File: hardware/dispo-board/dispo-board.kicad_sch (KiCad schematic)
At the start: 22 parts, among them SW1 SW_Push, U1 STM32H725RGV6, U2 TPS79633DCQ, Y1 32M

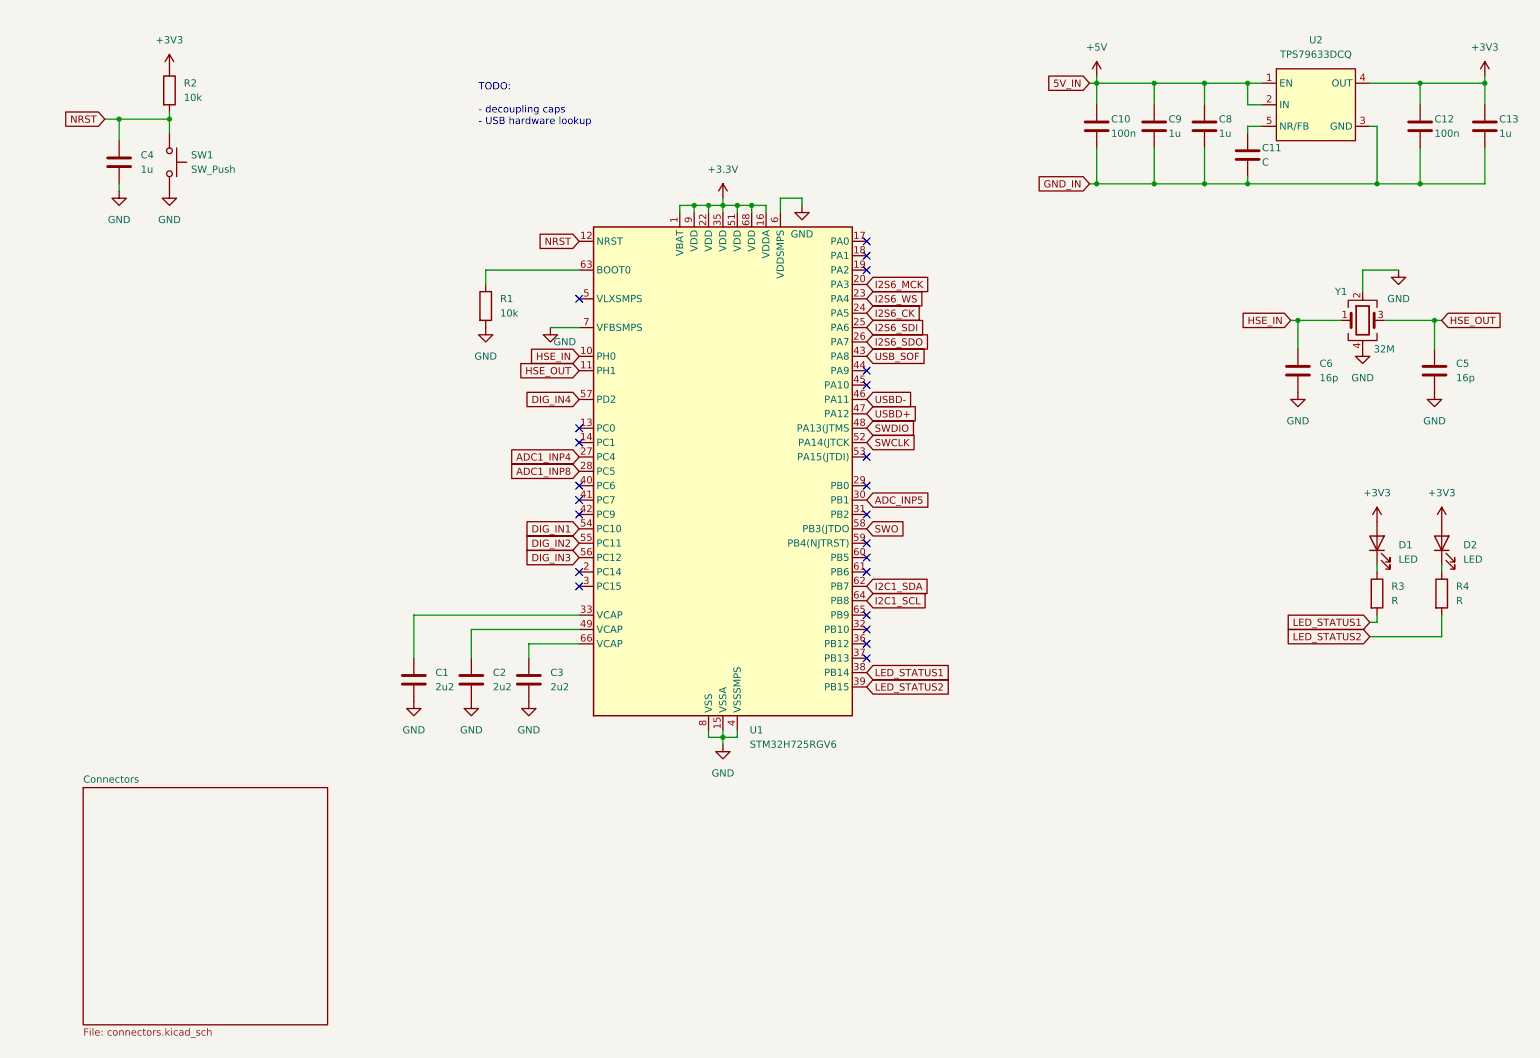
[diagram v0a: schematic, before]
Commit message: add decoupling caps, connectors, audio, minor corrections in report
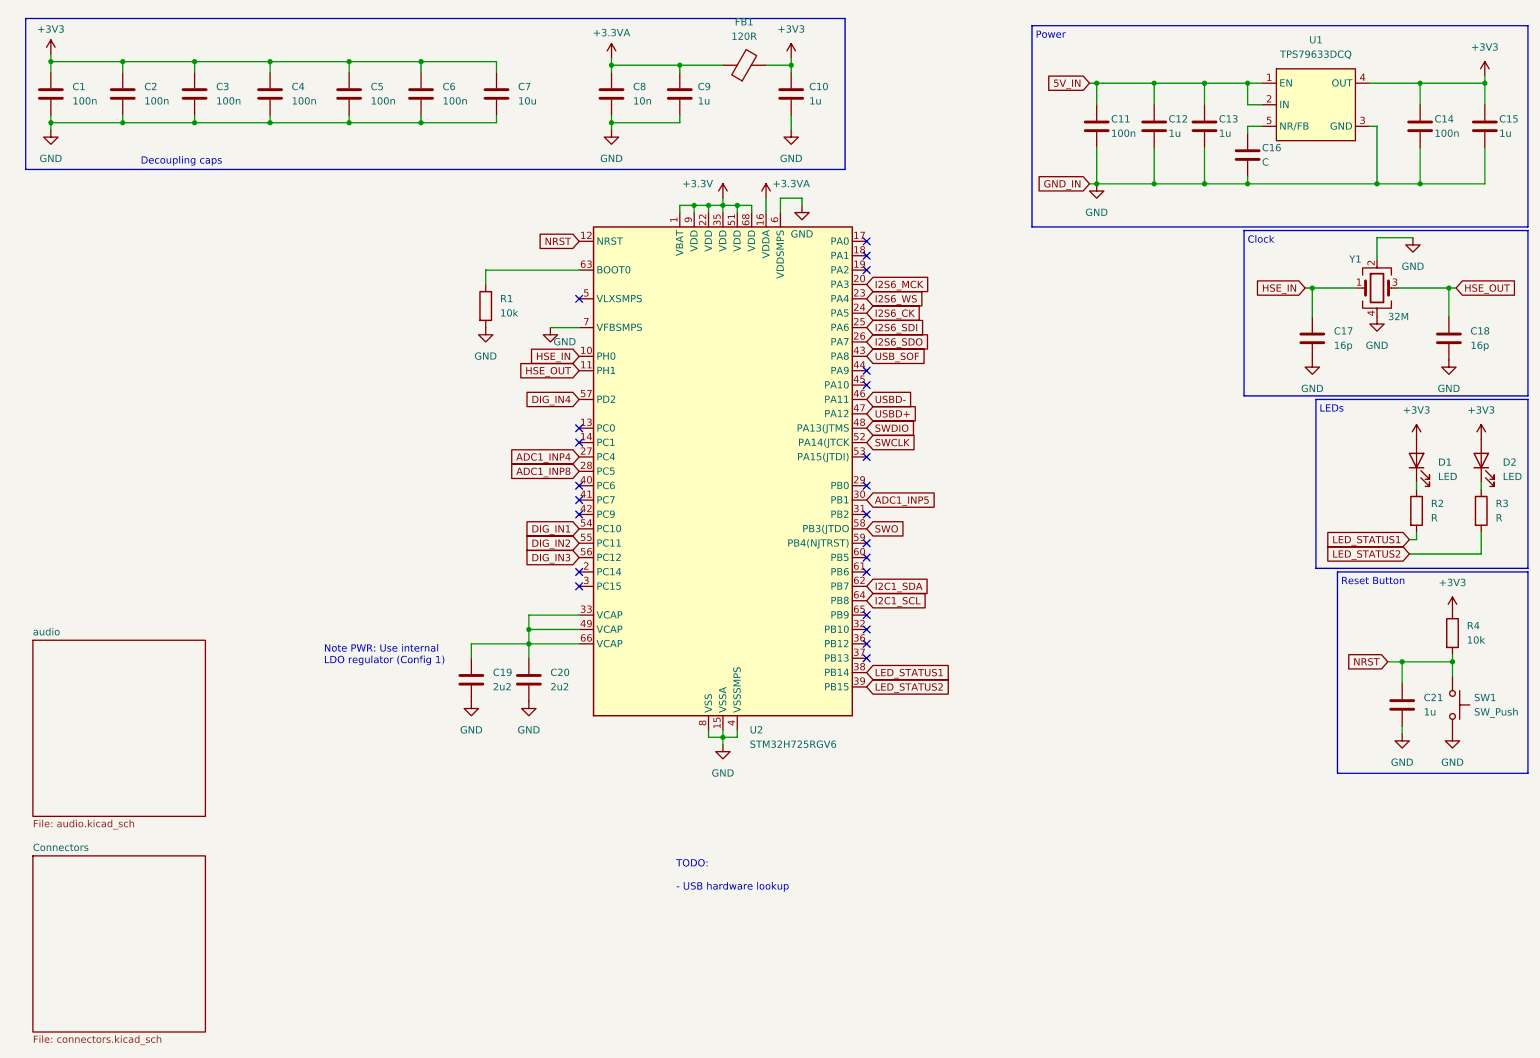
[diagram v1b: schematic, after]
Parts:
- added C10, C9: 1u, symbol Device:C
- added C2, C3, C4, C5, C6: 100n, symbol Device:C
- added C7: 10u, symbol Device:C
- added C8: 10n, symbol Device:C
- added FB1: 120R, symbol Device:FerriteBead
- C1: value 2u2 -> 100n
- renumbered C10 to C11, C9 to C12, C8 to C13, C12 to C14, C13 to C15, C11 to C16, C6 to C17, C5 to C18, C2 to C19, C3 to C20, C4 to C21, R3 to R2, R4 to R3, R2 to R4, U2 to U1, U1 to U2
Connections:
- net +3.3V: no longer U2.16 (VDDA)
- net +3V3: now also C1.1, C10.1, C2.1, C3.1, C4.1, C5.1, C6.1, C7.1, FB1.2
- net GND: now also C10.2, C2.2, C3.2, C4.2, C5.2, C6.2, C7.2, C8.2, C9.2
- net at C20.1, U2.66 (VCAP): now also C19.1, U2.33 (VCAP), U2.49 (VCAP)
- net +5V renamed 5V_IN
- net ADC_INP5 renamed ADC1_INP5
- new net +3.3VA: C8.1, C9.1, FB1.1, U2.16 (VDDA)
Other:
- added sheet audio (audio.kicad_sch)
- note added: "Clock"
- note added: "Decoupling caps"
- note added: "LEDs"
- note added: "Note PWR: Use internal LDO regulator (Config 1)"
- note added: "Power"
- note added: "Reset Button"
- note added: "TODO: - USB hardware lookup"
- note removed: "TODO: - decoupling caps - USB hardware lookup"
- moved on the sheet: C17, C18, C21, D1, D2, R2, R3, R4, SW1, Y1

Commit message: added analog frontend
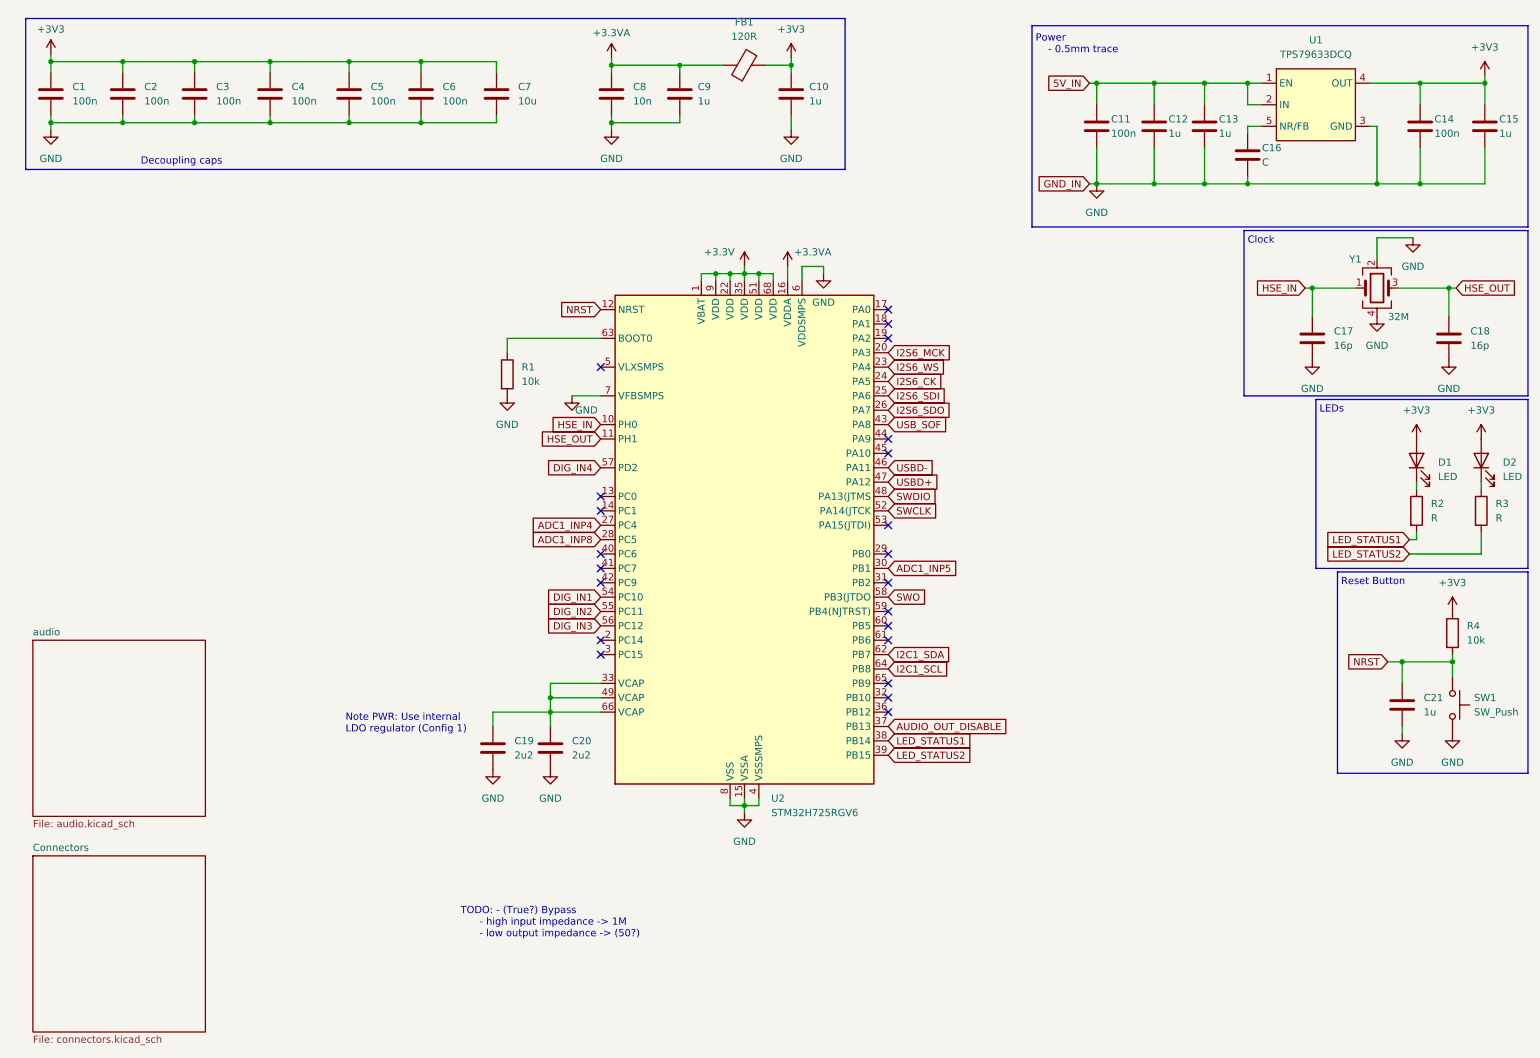
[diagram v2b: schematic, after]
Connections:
- net AUDIO_OUT_DISABLE: now reaches U2.37 (PB13)
- no-connect marks 23 -> 22
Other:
- note added: "Power - 0.5mm trace"
- note added: "TODO: - (True?) Bypass - high input impedance -> 1M - low output impedance -> (50?)"
- note removed: "Power"
- note removed: "TODO: - USB hardware lookup"
- moved on the sheet: C19, C20, R1, U2

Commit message: maybe final schematic?
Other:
- note removed: "TODO: - (True?) Bypass - high input impedance -> 1M - low output impedance -> (50?)"

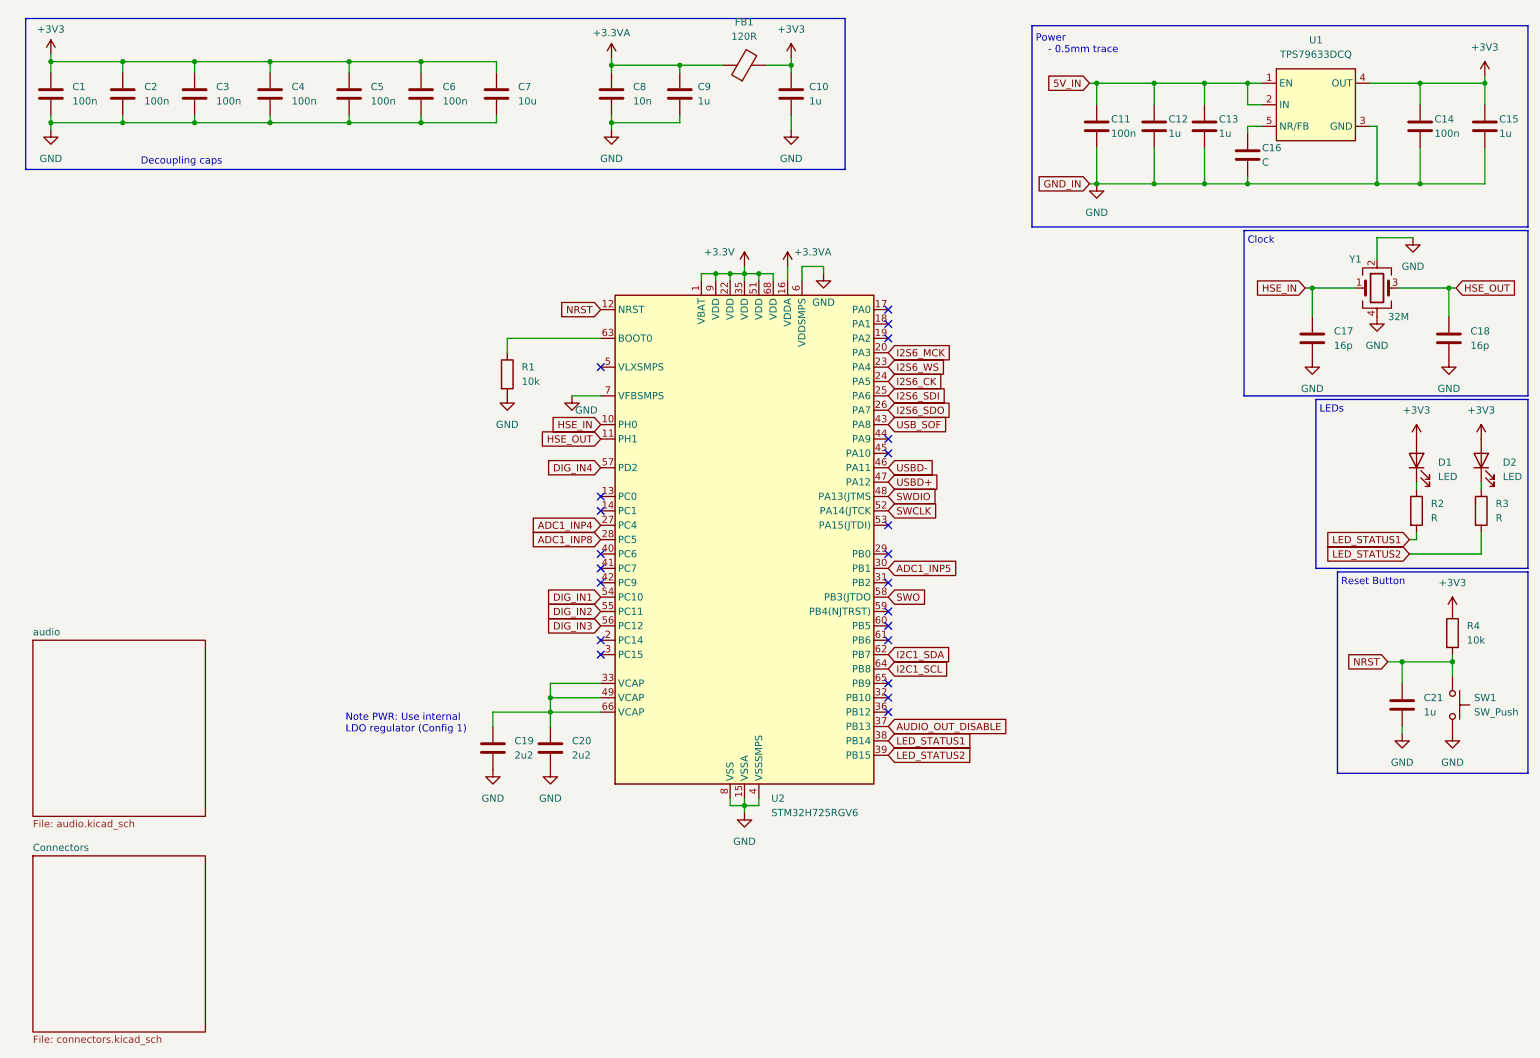
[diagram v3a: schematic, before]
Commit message: added debugger, corrected erc errors
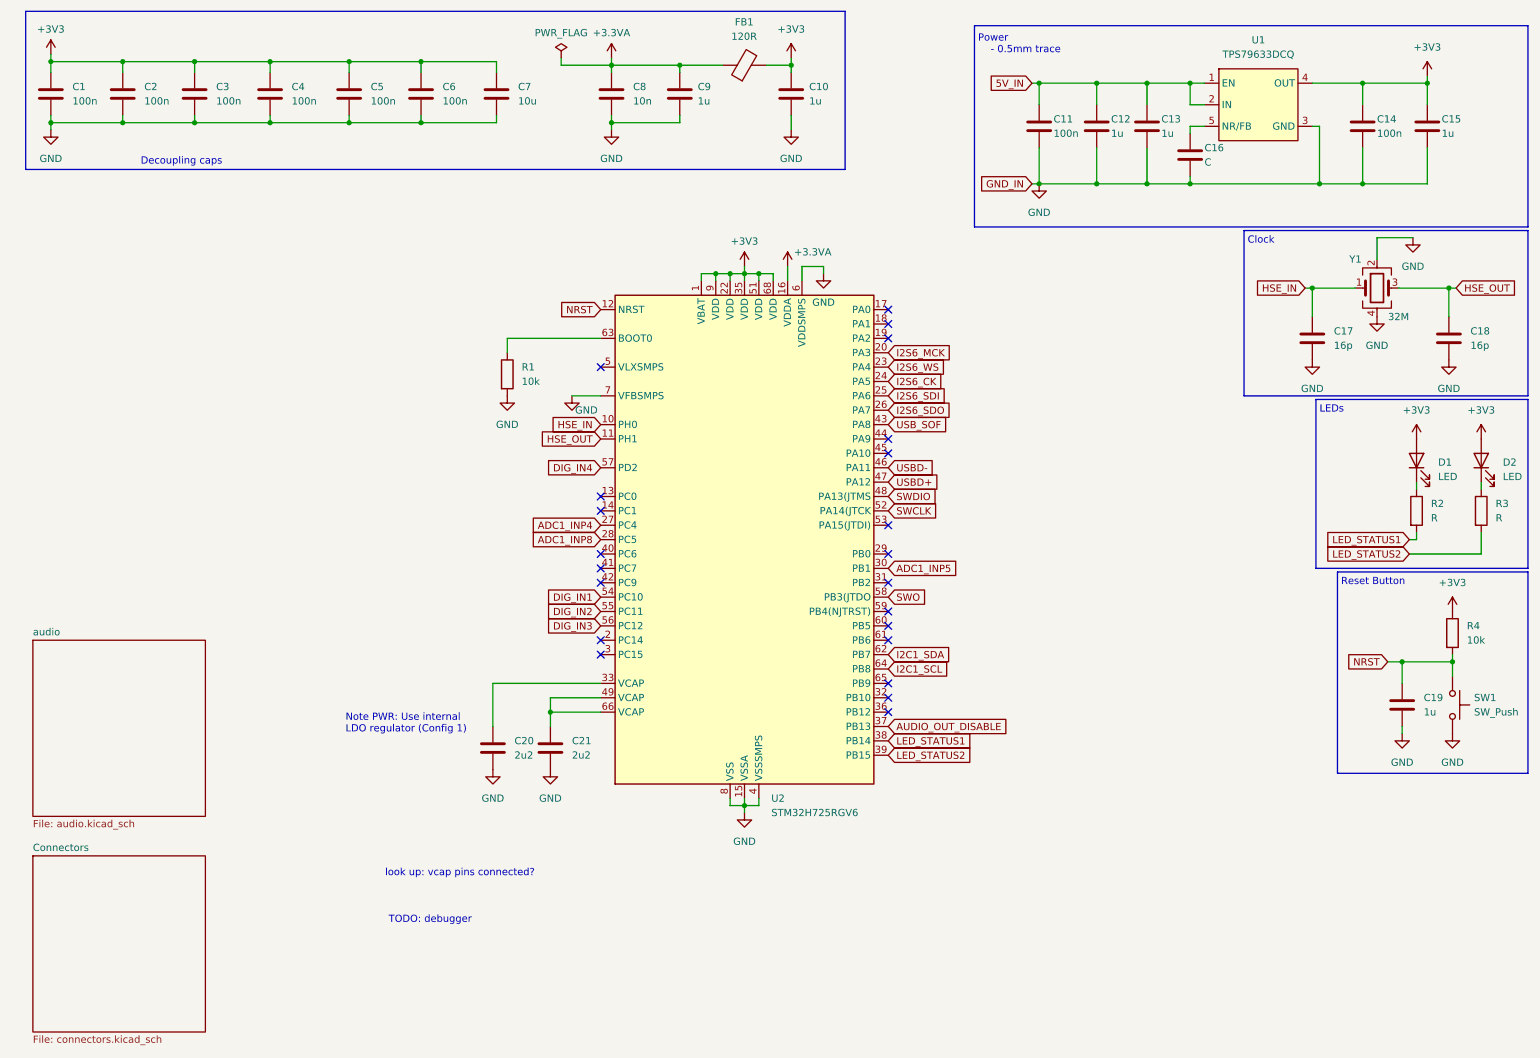
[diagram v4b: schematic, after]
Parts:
- renumbered C21 to C19, C19 to C20, C20 to C21
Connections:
- net +3.3V is gone; now on net +3V3: U2.1 (VBAT), U2.22 (VDD), U2.35 (VDD), U2.51 (VDD), U2.68 (VDD), U2.9 (VDD)
- net at C21.1, U2.49 (VCAP), U2.66 (VCAP): no longer C20.1, U2.33 (VCAP)
- new net: C20.1, U2.33 (VCAP)
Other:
- note added: "TODO: debugger"
- note added: "look up: vcap pins connected?"
- moved on the sheet: C11, C12, C13, C14, C15, C16, U1
